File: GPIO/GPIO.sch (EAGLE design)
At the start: 11 parts

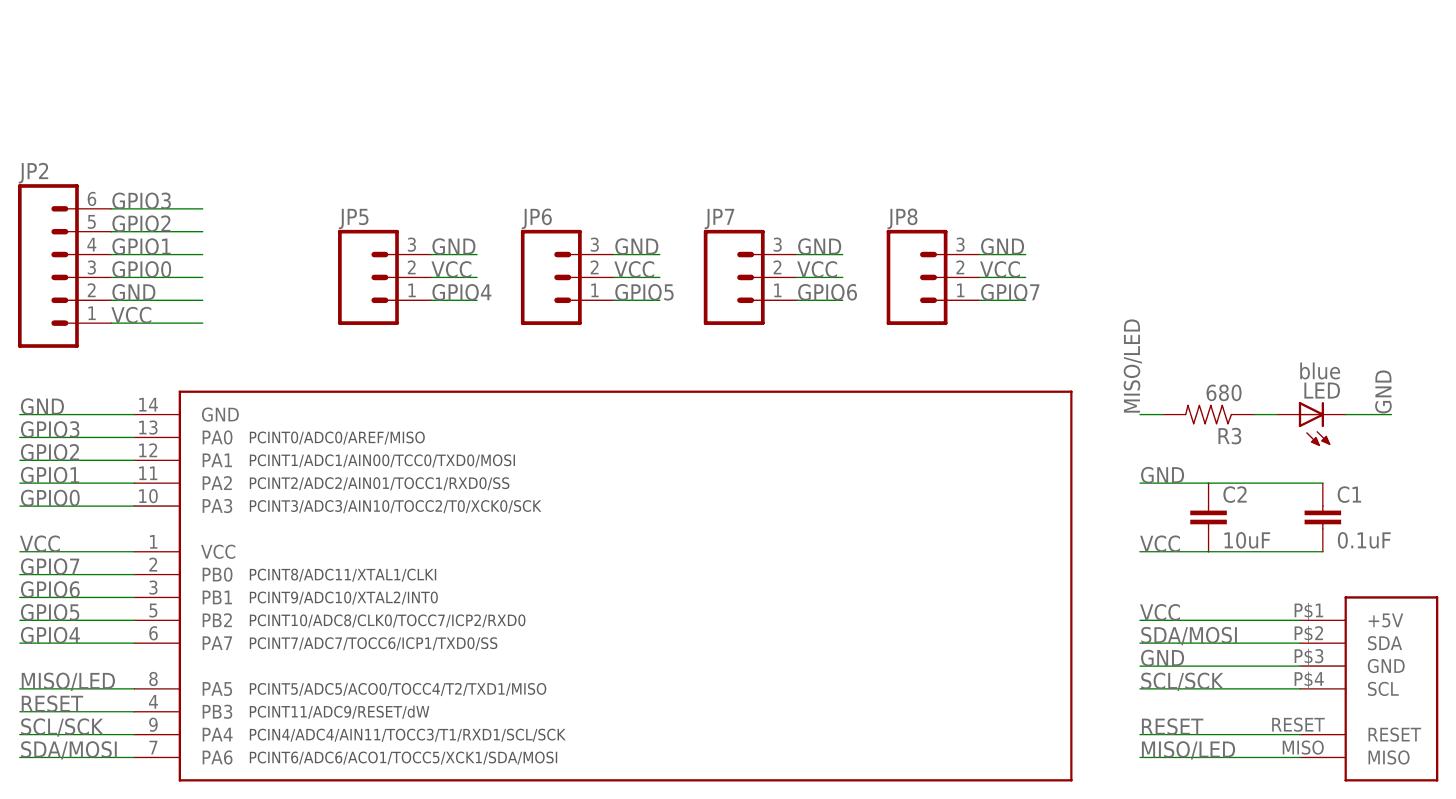
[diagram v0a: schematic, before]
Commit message: GPIO board rebuilt for v2 footprint
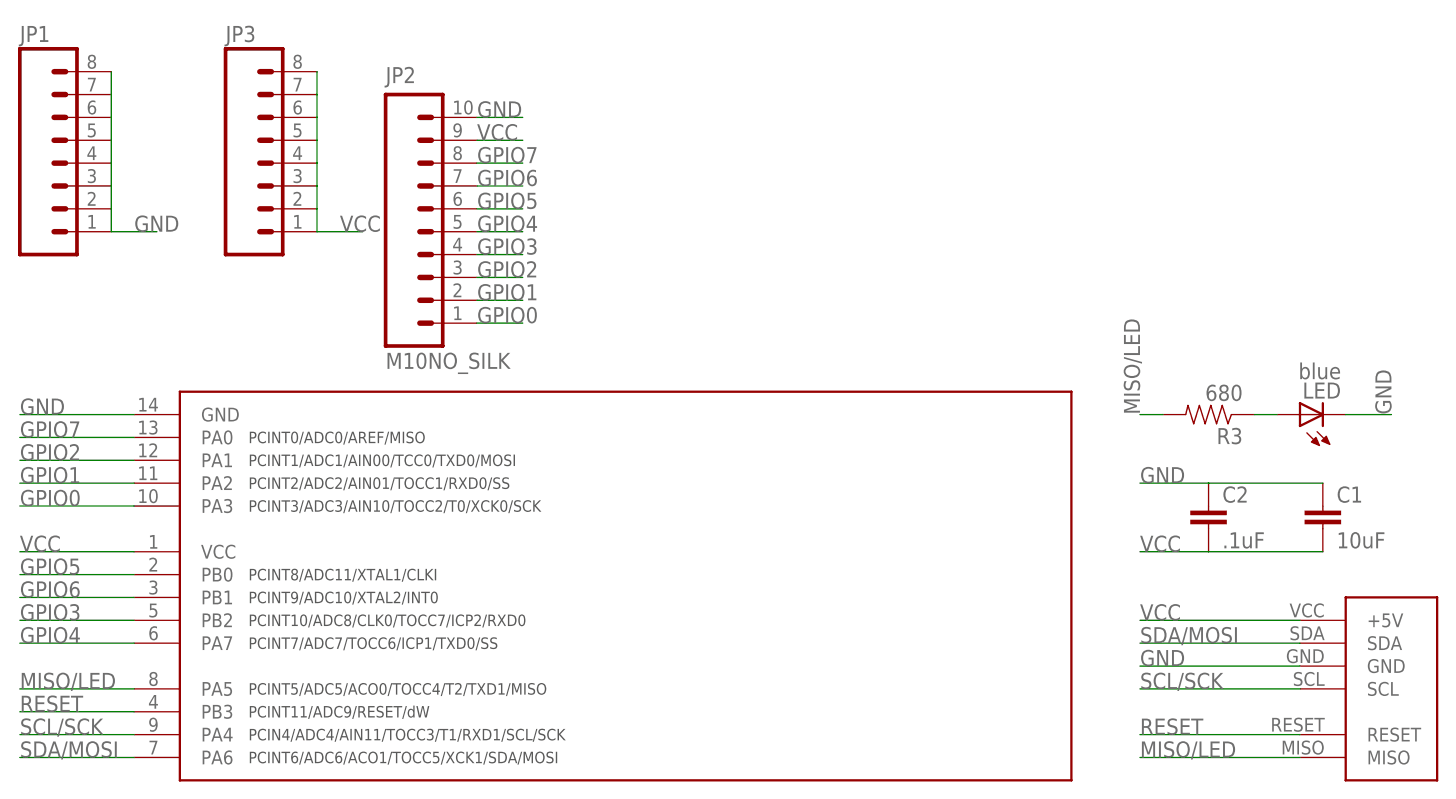
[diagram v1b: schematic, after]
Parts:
- removed JP5, JP6, JP7, JP8: (no value), SparkFun-Connectors:M03PTH
- added JP1, JP3: (no value), SparkFun-Connectors:M08NO_SILK
- C1: value 0.1uF -> 10uF
- C2: value 10uF -> .1uF
- JP2: value (none) -> M10NO_SILK; device SparkFun-Connectors:M06SIP -> SparkFun-Connectors:M10NO_SILK
- U$4: value FOOTPRINT -> FOOTPRINTFOOTPRINT-2; device IntegerLabs:FOOTPRINT -> IntegerLabs:FOOTPRINTFOOTPRINT-2
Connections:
- net GND: now also JP1.1, JP1.2, JP1.3, JP1.4, JP1.5, JP1.6, JP1.7, JP1.8, JP2.10; no longer JP2.2, JP5.3, JP6.3, JP7.3, JP8.3
- net GPIO0: now also JP2.1; no longer JP2.3
- net GPIO1: now also JP2.2; no longer JP2.4
- net GPIO2: now also JP2.3; no longer JP2.5
- net GPIO3: now also JP2.4, U$3.PB2; no longer JP2.6, U$3.PA0
- net GPIO4: now also JP2.5; no longer JP5.1
- net GPIO5: now also JP2.6, U$3.PB0; no longer JP6.1, U$3.PB2
- net GPIO6: now also JP2.7; no longer JP7.1
- net GPIO7: now also JP2.8, U$3.PA0; no longer JP8.1, U$3.PB0
- net VCC: now also JP2.9, JP3.1, JP3.2, JP3.3, JP3.4, JP3.5, JP3.6, JP3.7, JP3.8; no longer JP2.1, JP5.2, JP6.2, JP7.2, JP8.2

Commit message: Added current limiting resistors to io pins
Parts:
- added D1: DIODE-SCHOTTKY_, SparkFun-DiscreteSemi:DIODE-SCHOTTKY_
- added D2, D3, D6, D7: BAS70XY, diode:BAS70XY
- added R0A, R1A, R2A, R3A, R4A, R5A, R6A, R7A: (no value), SparkFun-Resistors:RESISTORPTH-1/4W-VERT
- added R0B, R1B, R2B, R3B, R4B, R5B, R6B, R7B: (no value), SparkFun-Resistors:RESISTOR0805-RES
- renumbered R3 to RLED
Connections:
- new net N$1: D2A.C2, D6A.C1A2
- new net N$2: D2B.C2, D6B.C1A2
- new net N$3: D3A.C2, D7A.C1A2
- new net P0: JP2.1, R0A.2, R0B.2
- new net P1: JP2.2, R1A.2, R1B.2
- new net P2: JP2.3, R2A.2, R2B.2
- new net P3: JP2.4, R3A.2, R3B.2
- new net P4: JP2.5, R4A.1, R4B.1
- new net P5: JP2.6, R5A.1, R5B.1
- new net P6: JP2.7, R6A.1, R6B.1
- new net P7: JP2.8, R7A.1, R7B.1
- new net VOUT: D1.C, JP2.9, JP3.1, JP3.2, JP3.3, JP3.4, JP3.5, JP3.6, JP3.7, JP3.8
- net GPIO0: now also R0A.1, R0B.1; no longer JP2.1
- net GPIO1: now also R1A.1, R1B.1; no longer JP2.2
- net GPIO2: now also R2A.1, R2B.1; no longer JP2.3
- net GPIO3: now also R3A.1, R3B.1; no longer JP2.4
- net GPIO4: now also R4A.2, R4B.2; no longer JP2.5
- net GPIO5: now also R5A.2, R5B.2; no longer JP2.6
- net GPIO6: now also R6A.2, R6B.2; no longer JP2.7
- net GPIO7: now also R7A.2, R7B.2; no longer JP2.8
- net VCC: now also D1.A; no longer JP2.9, JP3.1, JP3.2, JP3.3, JP3.4, JP3.5, JP3.6, JP3.7, JP3.8

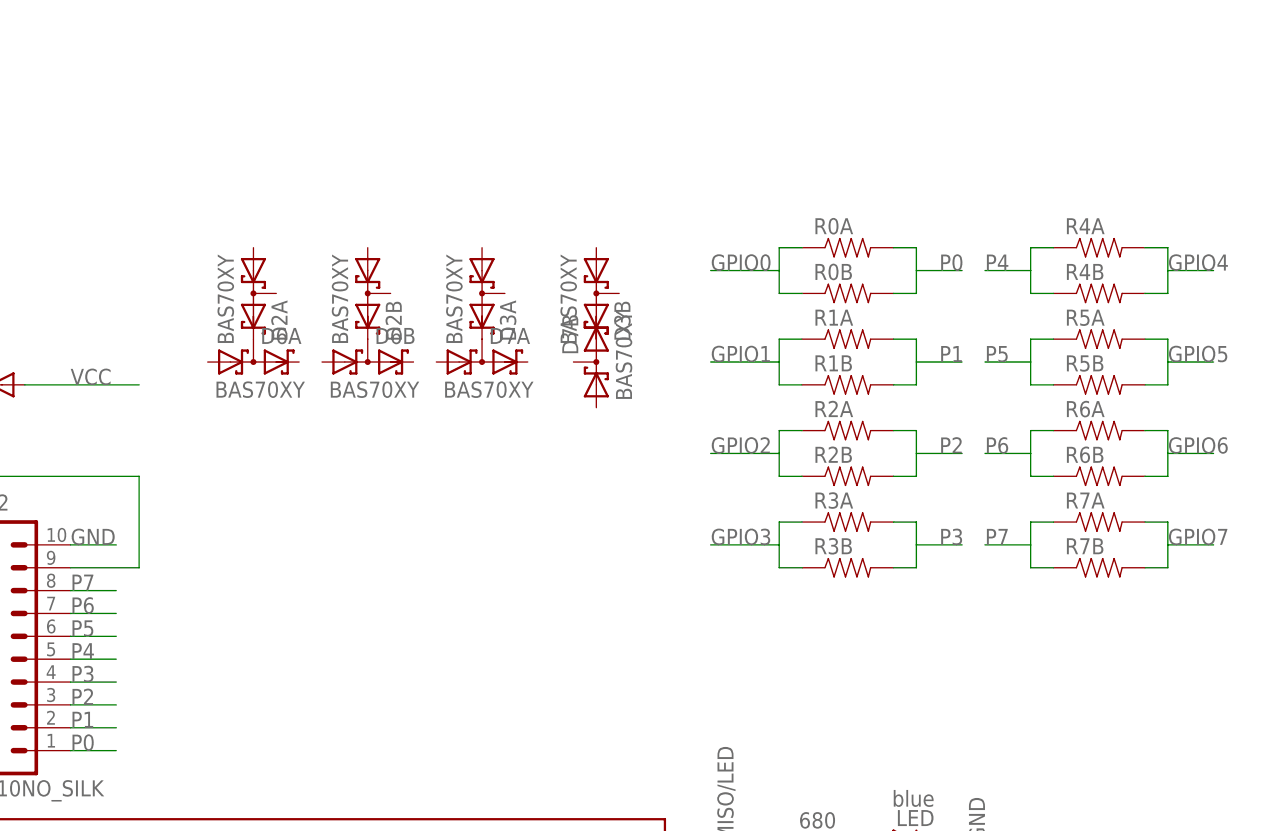
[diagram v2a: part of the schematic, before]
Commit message: Ruggedized GPIO board with current limiting resistors and clamping diodes.
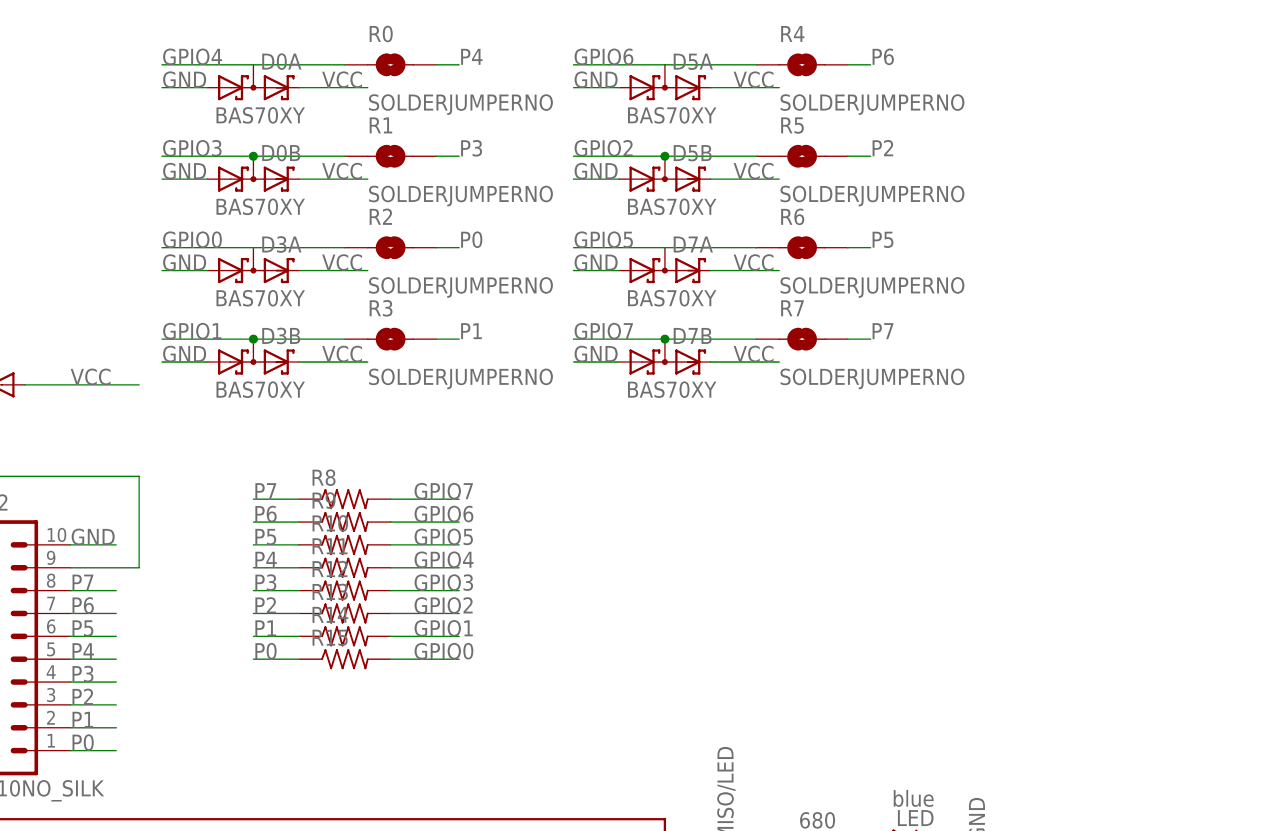
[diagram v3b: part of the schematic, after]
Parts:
- removed D2, D6: BAS70XY, diode:BAS70XY
- removed R0A, R1A, R2A, R3A, R4A, R5A, R6A, R7A: (no value), SparkFun-Resistors:RESISTORPTH-1/4W-VERT
- removed R0B, R1B, R2B, R3B, R4B, R5B, R6B, R7B: (no value), SparkFun-Resistors:RESISTOR0805-RES
- added D0, D5: BAS70XY, diode:BAS70XY
- added R0, R1, R2, R3, R4, R5, R6, R7: SOLDERJUMPERNO, SparkFun-Passives:SOLDERJUMPERNO
- added R10, R11, R12, R13, R14, R15, R8, R9: (no value), adafruit:R-US_R0805
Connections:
- removed net N$1: D2A.C2, D6A.C1A2
- removed net N$2: D2B.C2, D6B.C1A2
- removed net N$3: D3A.C2, D7A.C1A2
- net GND: now also D0A.A1, D0B.A1, D3A.A1, D3B.A1, D5A.A1, D5B.A1, D7A.A1, D7B.A1
- net GPIO0: now also D3A.C1A2, R15.2, R2.1; no longer R0A.1, R0B.1
- net GPIO1: now also D3B.C1A2, R14.2, R3.1; no longer R1A.1, R1B.1
- net GPIO2: now also D5B.C1A2, R13.2, R5.1; no longer R2A.1, R2B.1
- net GPIO3: now also D0B.C1A2, R1.1, R12.2; no longer R3A.1, R3B.1
- net GPIO4: now also D0A.C1A2, R0.1, R11.2; no longer R4A.2, R4B.2
- net GPIO5: now also D7A.C1A2, R10.2, R6.1; no longer R5A.2, R5B.2
- net GPIO6: now also D5A.C1A2, R4.1, R9.2; no longer R6A.2, R6B.2
- net GPIO7: now also D7B.C1A2, R7.1, R8.2; no longer R7A.2, R7B.2
- net P0: now also R15.1, R2.2; no longer R0A.2, R0B.2
- net P1: now also R14.1, R3.2; no longer R1A.2, R1B.2
- net P2: now also R13.1, R5.2; no longer R2A.2, R2B.2
- net P3: now also R1.2, R12.1; no longer R3A.2, R3B.2
- net P4: now also R0.2, R11.1; no longer R4A.1, R4B.1
- net P5: now also R10.1, R6.2; no longer R5A.1, R5B.1
- net P6: now also R4.2, R9.1; no longer R6A.1, R6B.1
- net P7: now also R7.2, R8.1; no longer R7A.1, R7B.1
- net VCC: now also D0A.C2, D0B.C2, D3A.C2, D3B.C2, D5A.C2, D5B.C2, D7A.C2, D7B.C2
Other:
- moved on the sheet: D3A, D3B, D7A, D7B

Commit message: Latest version of schematics and boards
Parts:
- removed C1: 10uF, SparkFun-Capacitors:CAP0805
- removed D0, D3, D5, D7: BAS70XY, diode:BAS70XY
- added D26, D27, D28, D29: BAS70XY, diode:BAS70XY
- C2: value .1uF -> .47uF
- R10, R11, R12, R13, R14, R15, R8, R9: value (none) -> 200; device adafruit:R-US_R0805 -> SparkFun-Resistors:RESISTOR0805-RES
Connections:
- net GND: now also D26A.A1, D26B.A1, D27A.A1, D27B.A1, D28A.A1, D28B.A1, D29A.A1, D29B.A1; no longer C1.1, D0A.A1, D0B.A1, D3A.A1, D3B.A1, D5A.A1, D5B.A1, D7A.A1, D7B.A1
- net GPIO0: now also D26A.C1A2; no longer D3A.C1A2
- net GPIO1: now also D26B.C1A2; no longer D3B.C1A2
- net GPIO2: now also D27A.C1A2; no longer D5B.C1A2
- net GPIO3: now also D27B.C1A2; no longer D0B.C1A2
- net GPIO4: now also D28A.C1A2; no longer D0A.C1A2
- net GPIO5: now also D28B.C1A2; no longer D7A.C1A2
- net GPIO6: now also D29A.C1A2; no longer D5A.C1A2
- net GPIO7: now also D29B.C1A2; no longer D7B.C1A2
- net SCL/SCK: now also U$4.SCK
- net SDA/MOSI: now also U$4.MOSI
- net VCC: now also D26A.C2, D26B.C2, D27A.C2, D27B.C2, D28A.C2, D28B.C2, D29A.C2, D29B.C2, U$4.VCC, U$4.VPROG; no longer C1.2, D0A.C2, D0B.C2, D3A.C2, D3B.C2, D5A.C2, D5B.C2, D7A.C2, D7B.C2, U$4.+5V
